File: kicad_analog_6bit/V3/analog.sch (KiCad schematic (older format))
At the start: 30 parts, among them P1 Conn_02x05_Odd_Even, P2 Conn_01x04, P3 Conn_01x06, P4 Conn_01x02, P6 Conn_01x01, P7 Conn_01x01, U1 MAX9144, U2 MAX9144, U3 DG441xY, U4 MAX5259EEE+, U5 MCP1754S-3302xCB

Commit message: Analog V3 non-inverted 14 pin
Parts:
- removed U3: DG441xY, Package_SO:SOIC-16_3.9x9.9mm_P1.27mm, symbol Analog_Switch:DG441xY
- added R10, R9: 1K, Resistor_SMD:R_0805_2012Metric_Pad1.15x1.40mm_HandSolder, symbol Device:R_Small
- added U3: 4066, Package_SO:SOIC-14_3.9x8.7mm_P1.27mm, symbol 4xxx:4066
- R1: value 150R -> 75R
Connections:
- wire segments 167 -> 166
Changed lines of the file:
@@
 Wire Wire Line
 	6450 4150 7000 4150
-Text Label 2400 6500 0    50   ~ 0
+Text Label 1400 6500 2    50   ~ 0
 GND
 Text Label 2400 5300 2    50   ~ 0
@@
 Wire Wire Line
 	6400 7550 6450 7550
-Text Label 1050 2350 2    50   ~ 0
+$Comp
+L 4xxx:4066 U3
+U 5 1 5E118FBF
+P 9050 5900
+F 0 "U3" H 9280 5946 50  0000 L CNN
+F 1 "4066" H 9280 5855 50  0000 L CNN
+F 2 "Package_SO:SOIC-14_3.9x8.7mm_P1.27mm" H 9050 5900 50  0001 C CNN
+F 3 "http://www.ti.com/lit/ds/symlink/cd4066b.pdf" H 9050 5900 50  0001 C CNN
+	5    9050 5900
+	1    0    0    -1
+$EndComp
+Text Label 9050 5400 2    50   ~ 0
 VCC
-Text Label 1050 3350 2    50   ~ 0
-GND
+Text Label 9050 6400 2    50   ~ 0
+GND
+$Comp
+L 4xxx:4066 U3
+U 1 1 5E1234E2
+P 2400 3550
+F 0 "U3" V 2354 3422 50  0000 R CNN
+F 1 "4066" V 2445 3422 50  0000 R CNN
+F 2 "Package_SO:SOIC-14_3.9x8.7mm_P1.27mm" H 2400 3550 50  0001 C CNN
+F 3 "http://www.ti.com/lit/ds/symlink/cd4066b.pdf" H 2400 3550 50  0001 C CNN
+	1    2400 3550
+	0    -1   1    0
+$EndComp
+$Comp
+L 4xxx:4066 U3
+U 2 1 5E127744
+P 4600 3550
+F 0 "U3" V 4554 3422 50  0000 R CNN
+F 1 "4066" V 4645 3422 50  0000 R CNN
+F 2 "Package_SO:SOIC-14_3.9x8.7mm_P1.27mm" H 4600 3550 50  0001 C CNN
+F 3 "http://www.ti.com/lit/ds/symlink/cd4066b.pdf" H 4600 3550 50  0001 C CNN
+	2    4600 3550
+	0    1    1    0
+$EndComp
+$Comp
+L 4xxx:4066 U3
+U 3 1 5E129BF6
+P 3150 3550
+F 0 "U3" V 3104 3422 50  0000 R CNN
+F 1 "4066" V 3195 3422 50  0000 R CNN
+F 2 "Package_SO:SOIC-14_3.9x8.7mm_P1.27mm" H 3150 3550 50  0001 C CNN
+F 3 "http://www.ti.com/lit/ds/symlink/cd4066b.pdf" H 3150 3550 50  0001 C CNN
+	3    3150 3550
+	0    1    1    0
+$EndComp
 Wire Wire Line
 	2400 3850 2400 5050
@@
 	3150 4200 3450 4200
 Wire Wire Line
+	3900 4200 3900 3850
+Wire Wire Line
+	3900 4200 4200 4200
+Wire Wire Line
 	4600 4200 4600 3850
+Connection ~ 3900 4200
 Text Label 2950 4200 2    50   ~ 0
 GND
@@
 P 2400 3000
 F 0 "R1" H 2150 3050 50  0000 L CNN
-F 1 "150R" H 2100 2950 50  0000 L CNN
+F 1 "75R" H 2100 2950 50  0000 L CNN
 F 2 "Resistor_SMD:R_0805_2012Metric_Pad1.15x1.40mm_HandSolder" H 2400 3000 50  0001 C CNN
 F 3 "~" H 2400 3000 50  0001 C CNN
@@
 Connection ~ 3450 4200
 Wire Wire Line
+	3450 4200 3900 4200
+Wire Wire Line
 	4200 4100 4200 4200
 Connection ~ 4200 4200
@@
 Wire Wire Line
 	4200 3900 4200 3800
+Connection ~ 3450 3550
+Wire Wire Line
+	3450 3550 3450 3800
 Wire Wire Line
 	4050 3800 4200 3800
+Connection ~ 4200 3800
+Wire Wire Line
+	4200 3800 4200 3550
 Wire Wire Line
 	3150 3250 3150 2450
 Connection ~ 3150 2450
 Wire Wire Line
+	3900 3250 3900 2100
+Wire Wire Line
 	4600 3250 4600 1750
 Connection ~ 4600 1750
 Wire Wire Line
+	3450 3100 3450 3550
+Wire Wire Line
 	3450 3100 4900 3100
 Wire Wire Line
@@
 Wire Wire Line
 	800  5200 800  3550
+Wire Wire Line
+	800  3550 2100 3550
 Wire Wire Line
 	1100 4450 1100 4650
@@
 Text Label 2900 6100 0    50   ~ 0
 SPARE
-Text Label 2400 3200 0    50   ~ 0
+Text Label 2400 3250 0    50   ~ 0
 SW_CLAMP
 Text Label 1950 4850 0    50   ~ 0
@@
 	1    0    0    -1
 $EndComp
+$Comp
+L 4xxx:4066 U3
+U 4 1 5E12E54E
+P 3900 3550
+F 0 "U3" V 3854 3422 50  0000 R CNN
+F 1 "4066" V 3945 3422 50  0000 R CNN
+F 2 "Package_SO:SOIC-14_3.9x8.7mm_P1.27mm" H 3900 3550 50  0001 C CNN
+F 3 "http://www.ti.com/lit/ds/symlink/cd4066b.pdf" H 3900 3550 50  0001 C CNN
+	4    3900 3550
+	0    1    1    0
+$EndComp
 Wire Wire Line
 	950  6000 1500 6000
@@
 Wire Wire Line
 	1500 6000 1900 6000
-Wire Wire Line
-	3450 3100 3450 3550
-Wire Wire Line
-	3450 4200 3900 4200
-Wire Wire Line
-	3900 4200 3900 3850
-Connection ~ 3900 4200
-Wire Wire Line
-	3900 4200 4200 4200
-Wire Wire Line
-	4800 3550 4900 3550
-Wire Wire Line
-	4200 3800 4200 3550
-Wire Wire Line
-	4200 3550 4100 3550
-Connection ~ 4200 3800
-Wire Wire Line
-	3350 3550 3450 3550
-Connection ~ 3450 3550
-Wire Wire Line
-	3450 3550 3450 3800
-Wire Wire Line
-	3900 2100 3900 3250
-Wire Wire Line
-	800  3550 2200 3550
-Wire Wire Line
-	1400 2350 1300 2350
-Connection ~ 1300 2350
-Wire Wire Line
-	1300 2350 1050 2350
-Wire Wire Line
-	1400 3350 1300 3350
-Connection ~ 1300 3350
-Wire Wire Line
-	1300 3350 1050 3350
-$Comp
-L Analog_Switch:DG441xY U3
-U 5 1 5E5EA56F
-P 1300 2850
-F 0 "U3" H 1580 2896 50  0000 L CNN
-F 1 "DG441xY" H 1580 2805 50  0000 L CNN
-F 2 "Package_SO:SOIC-16_3.9x9.9mm_P1.27mm" H 1300 2750 50  0001 C CNN
-F 3 "https://datasheets.maximintegrated.com/en/ds/DG441-DG442.pdf" H 1300 2850 50  0001 C CNN
-	5    1300 2850
-	1    0    0    -1
-$EndComp
-$Comp
-L Analog_Switch:DG441xY U3
-U 4 1 5E5EE151
-P 3900 3550
-F 0 "U3" V 3946 3680 50  0000 L CNN
-F 1 "DG441xY" V 3855 3680 50  0000 L CNN
-F 2 "Package_SO:SOIC-16_3.9x9.9mm_P1.27mm" H 3900 3450 50  0001 C CNN
-F 3 "https://datasheets.maximintegrated.com/en/ds/DG441-DG442.pdf" H 3900 3550 50  0001 C CNN
-	4    3900 3550
-	0    -1   -1   0
-$EndComp
-$Comp
-L Analog_Switch:DG441xY U3
-U 1 1 5E5EFEBA
-P 2400 3550
-F 0 "U3" V 2500 3250 50  0000 L CNN
-F 1 "DG441xY" V 2650 3050 50  0000 L CNN
-F 2 "Package_SO:SOIC-16_3.9x9.9mm_P1.27mm" H 2400 3450 50  0001 C CNN
-F 3 "https://datasheets.maximintegrated.com/en/ds/DG441-DG442.pdf" H 2400 3550 50  0001 C CNN
-	1    2400 3550
-	0    1    1    0
-$EndComp
-$Comp
-L Analog_Switch:DG441xY U3
-U 2 1 5E5F16C1
-P 4600 3550
-F 0 "U3" V 4646 3680 50  0000 L CNN
-F 1 "DG441xY" V 4555 3680 50  0000 L CNN
-F 2 "Package_SO:SOIC-16_3.9x9.9mm_P1.27mm" H 4600 3450 50  0001 C CNN
-F 3 "https://datasheets.maximintegrated.com/en/ds/DG441-DG442.pdf" H 4600 3550 50  0001 C CNN
-	2    4600 3550
-	0    -1   -1   0
-$EndComp
-$Comp
-L Analog_Switch:DG441xY U3
-U 3 1 5E5F2F3B
-P 3150 3550
-F 0 "U3" V 3196 3680 50  0000 L CNN
-F 1 "DG441xY" V 3105 3680 50  0000 L CNN
-F 2 "Package_SO:SOIC-16_3.9x9.9mm_P1.27mm" H 3150 3450 50  0001 C CNN
-F 3 "https://datasheets.maximintegrated.com/en/ds/DG441-DG442.pdf" H 3150 3550 50  0001 C CNN
-	3    3150 3550
-	0    -1   -1   0
-$EndComp
-Wire Wire Line
-	1400 2350 1400 2450
+$Comp
+L Device:R_Small R9
+U 1 1 5E6BC038
+P 1500 6300
+F 0 "R9" H 1350 6350 50  0000 L CNN
+F 1 "1K" H 1350 6250 50  0000 L CNN
+F 2 "Resistor_SMD:R_0805_2012Metric_Pad1.15x1.40mm_HandSolder" H 1500 6300 50  0001 C CNN
+F 3 "~" H 1500 6300 50  0001 C CNN
+	1    1500 6300
+	1    0    0    -1
+$EndComp
+$Comp
+L Device:R_Small R10
+U 1 1 5E6BCBE0
+P 1650 6300
+F 0 "R10" H 1709 6346 50  0000 L CNN
+F 1 "1K" H 1709 6255 50  0000 L CNN
+F 2 "Resistor_SMD:R_0805_2012Metric_Pad1.15x1.40mm_HandSolder" H 1650 6300 50  0001 C CNN
+F 3 "~" H 1650 6300 50  0001 C CNN
+	1    1650 6300
+	1    0    0    -1
+$EndComp
+Wire Wire Line
+	1500 6000 1500 6200
+Wire Wire Line
+	1650 5900 1650 6200
+Wire Wire Line
+	2400 6500 1650 6500
+Wire Wire Line
+	1500 6500 1500 6400
+Wire Wire Line
+	1650 6400 1650 6500
+Connection ~ 1650 6500
+Wire Wire Line
+	1650 6500 1500 6500
+Wire Wire Line
+	1500 6500 1400 6500
+Connection ~ 1500 6500
 $EndSCHEMATC

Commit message: V3 PCB layout with MAX4610
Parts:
- added J1: Spare DAC, TestPoint:TestPoint_Pad_D1.0mm, symbol Connector_Generic:Conn_01x01
- U1, U2: value MAX9144 -> MAX9108; symbol Comparator:MAX9144 -> analog-rescue:MAX9108-Comparator
- U3: value 4066 -> MAX4610; symbol 4xxx:4066 -> analog-rescue:MAX4610-4xxx
- renumbered C8 to C4, C9 to C5, C5 to C7, C7 to C8, C4 to C9, CL1 to Cx1, R3 to R1, R9 to R3, R10 to R4, R8 to R5, R7 to R6, R4 to R7, R5 to R8, R6 to R9, R1 to Rx1
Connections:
- wire segments 166 -> 171

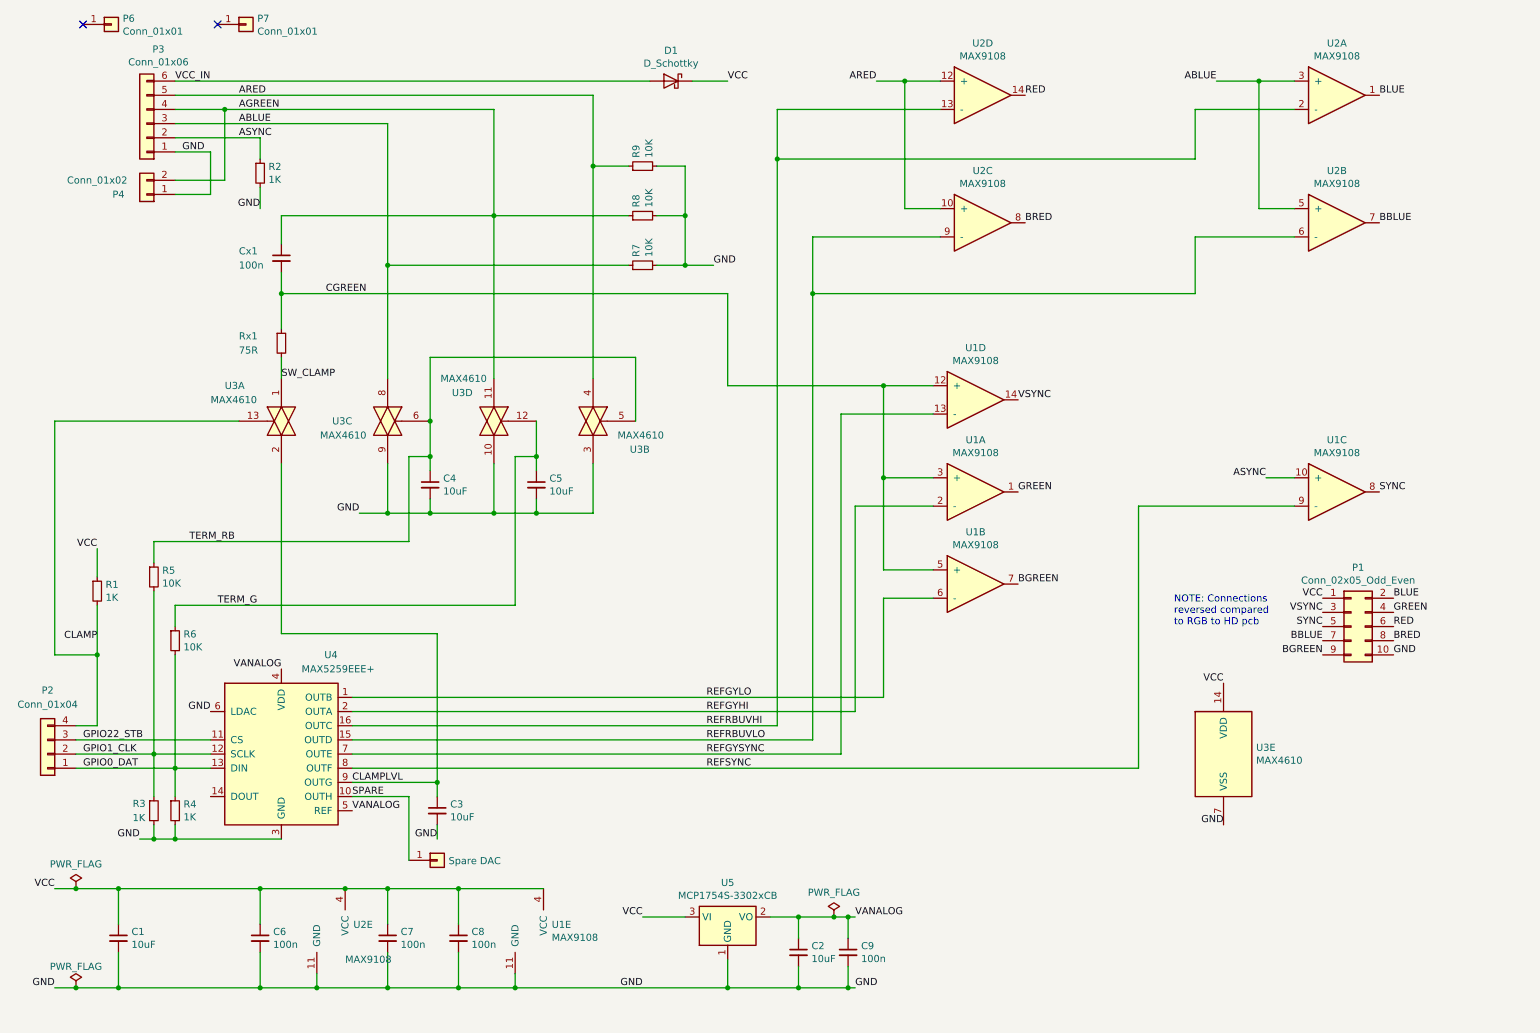
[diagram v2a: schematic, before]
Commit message: Update pcb with AC/DC switch
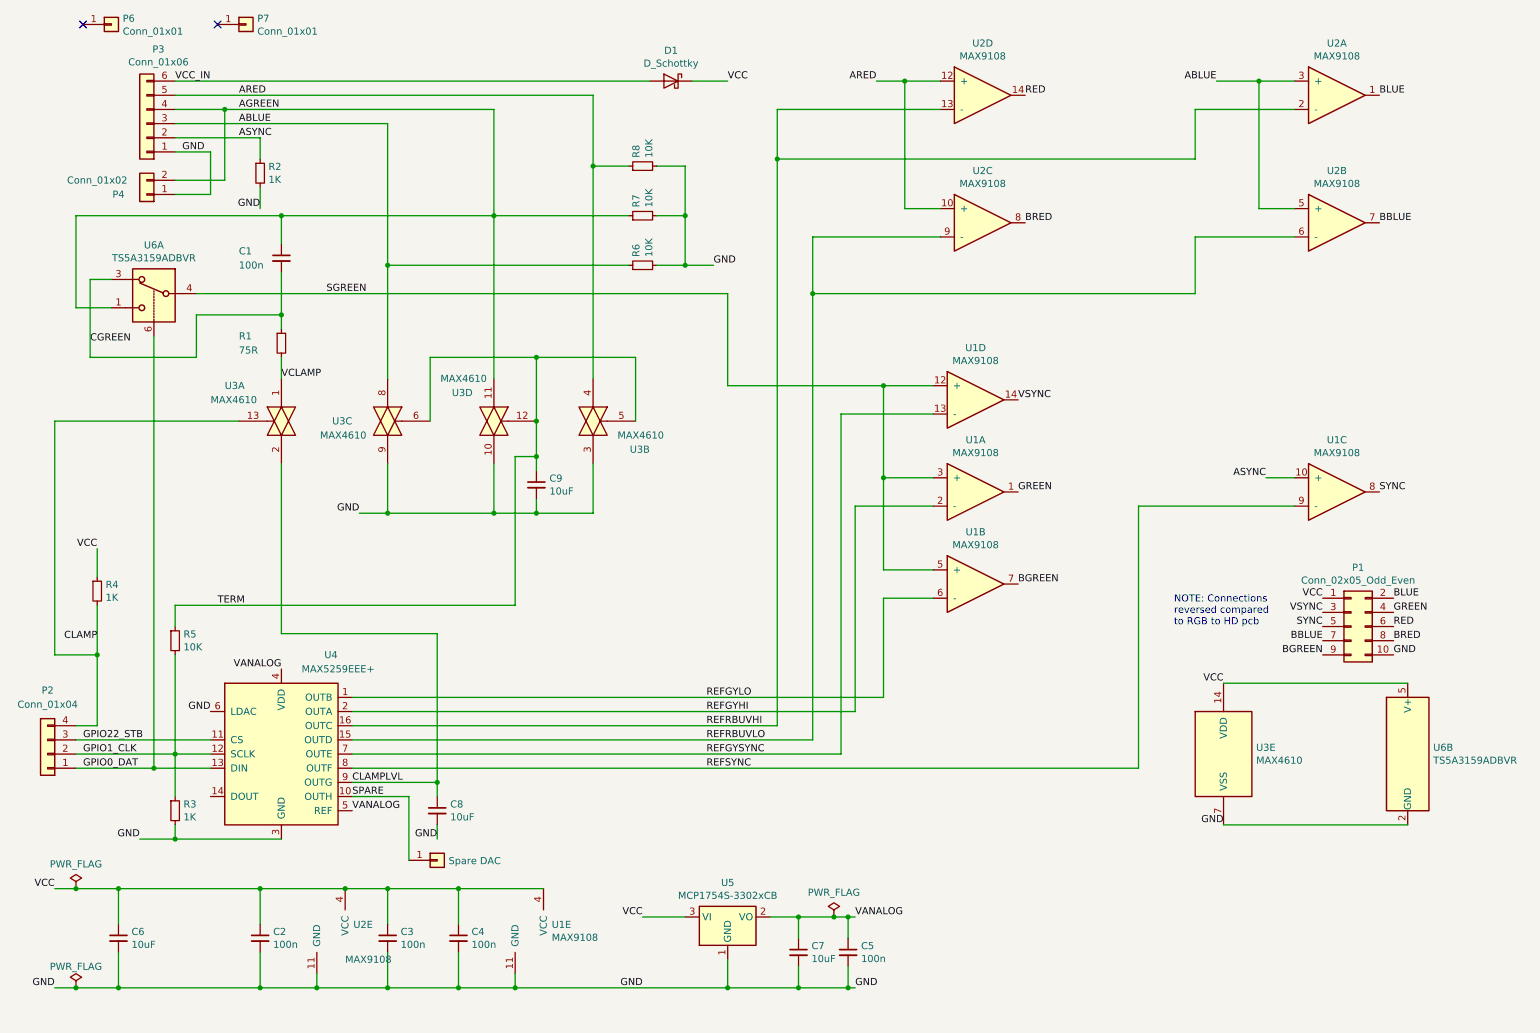
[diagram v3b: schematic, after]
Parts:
- removed C4: 10uF, Capacitor_SMD:C_0805_2012Metric_Pad1.15x1.40mm_HandSolder, symbol Device:C_Small
- removed R3: 1K, Resistor_SMD:R_0805_2012Metric_Pad1.15x1.40mm_HandSolder, symbol Device:R_Small
- removed R5: 10K, Resistor_SMD:R_0805_2012Metric_Pad1.15x1.40mm_HandSolder, symbol Device:R_Small
- added U6: TS5A3159ADBVR, Package_TO_SOT_SMD:SOT-23-6_Handsoldering, symbol Analog_Switch:TS5A3159ADBVR
- renumbered Cx1 to C1, C6 to C2, C7 to C3, C8 to C4, C9 to C5, C1 to C6, C2 to C7, C3 to C8, C5 to C9, Rx1 to R1, R4 to R3, R1 to R4, R6 to R5, R7 to R6, R8 to R7, R9 to R8
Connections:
- net TERM_RB is gone; now on net TERM: U3.5, U3.6
- net AGREEN: now also U6.1
- net CGREEN: now also U6.3; no longer U1.12 (+), U1.3 (+), U1.5 (+)
- net GND: now also U6.2 (GND)
- net GPIO0_DAT: now also U6.6; no longer R3.1, R5.2
- net GPIO1_CLK: now also R3.1, R5.2
- net VCC: now also U6.5 (V+)
- net SW_CLAMP renamed VCLAMP
- net TERM_G renamed TERM
- new net SGREEN: U1.12 (+), U1.3 (+), U1.5 (+), U6.4

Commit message: V3 pcb plus some older alternatives
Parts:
- removed J1: Spare DAC, TestPoint:TestPoint_Pad_D1.0mm, symbol Connector_Generic:Conn_01x01
- removed P1: Conn_02x05_Odd_Even, Connector_PinSocket_2.54mm:PinSocket_2x05_P2.54mm_Horizontal, symbol Connector_Generic:Conn_02x05_Odd_Even
- removed P4: Conn_01x02, Connector_PinHeader_2.54mm:PinHeader_1x02_P2.54mm_Vertical, symbol Connector_Generic:Conn_01x02
- added JP1, JP2: SolderJumper_3_Bridged12, Jumper:SolderJumper-3_P1.3mm_Bridged12_RoundedPad1.0x1.5mm, symbol Jumper:SolderJumper_3_Bridged12
- added P1: Conn_02x06_Odd_Even, Connector_PinSocket_2.54mm:PinSocket_2x06_P2.54mm_Horizontal, symbol Connector_Generic:Conn_02x06_Odd_Even
- added R10, R11, R9: 68R, Resistor_SMD:R_0805_2012Metric_Pad1.15x1.40mm_HandSolder, symbol Device:R_Small
- added U7: MAX9108-Comparator, Package_SO:SOIC-14_3.9x8.7mm_P1.27mm, symbol analog-rescue:MAX9108-Comparator
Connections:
- net ABLUE: now also R9.1, U7.10 (+), U7.12 (+); no longer U3.8
- net AGREEN: now also U6.3, R10.1; no longer U3.11, U6.1
- net ARED: now also R11.1, U7.3 (+), U7.5 (+); no longer U3.4
- net BBLUE: now also P1.7 (Pin_7)
- net BGREEN: now also P1.9 (Pin_9)
- net BLUE: now also P1.2 (Pin_2)
- net BRED: now also P1.8 (Pin_8)
- net CGREEN: now also U6.1; no longer U6.3
- net CLAMPLVL: now also U7.6 (-), U7.9 (-)
- net GND: now also P1.10 (Pin_10), U7.11 (GND)
- net GREEN: now also P1.4 (Pin_4)
- net RED: now also P1.6 (Pin_6)
- net SPARE: now also U7.13 (-), U7.2 (-)
- net SYNC: now also P1.5 (Pin_5)
- net VCC: now also P1.1 (Pin_1), U7.4 (VCC)
- net VSYNC: now also P1.3 (Pin_3)
- new net: R11.2, U3.4
- new net: R9.2, U3.8
- new net: R10.2, U3.11
- new net: JP1.1 (A), U7.14
- new net: JP1.3 (B), U7.1
- new net: JP2.1 (A), U7.7
- new net: JP2.3 (B), U7.8
- new net UV1: JP1.2 (C), P1.11 (Pin_11)
- new net UV2: JP2.2 (C), P1.12 (Pin_12)
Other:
- moved on the sheet: C8, U1C, U2B, U2C

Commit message: Updated analog board
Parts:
- R10, R11, R9: value 68R -> 75R
- R6, R7, R8: value 10K -> 47K
- U3: value MAX4610 -> TS12A44514DR; symbol analog-rescue:MAX4610-4xxx -> analog-rescue:TS12A44514DR-4xxx
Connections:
- net UV1: now also JP2.2 (C), P1.12 (Pin_12); no longer JP1.2 (C), P1.11 (Pin_11)
- net UV2: now also JP1.2 (C), P1.11 (Pin_11); no longer JP2.2 (C), P1.12 (Pin_12)
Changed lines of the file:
@@
 	6400 7550 6450 7550
 $Comp
-L analog-rescue:MAX4610-4xxx U3
+L analog-rescue:TS12A44514DR-4xxx U3
 U 5 1 5E118FBF
 P 9050 5900
 F 0 "U3" H 9280 5946 50  0000 L CNN
-F 1 "MAX4610" H 9280 5855 50  0000 L CNN
+F 1 "TS12A44514DR" H 9280 5855 50  0000 L CNN
 F 2 "Package_SO:SOIC-14_3.9x8.7mm_P1.27mm" H 9050 5900 50  0001 C CNN
-F 3 "http://www.ti.com/lit/ds/symlink/cdMAX4610b.pdf" H 9050 5900 50  0001 C CNN
+F 3 "http://www.ti.com/lit/ds/symlink/cdTS12A44514DRb.pdf" H 9050 5900 50  0001 C CNN
 	5    9050 5900
 	1    0    0    -1
@@
 GND
 $Comp
-L analog-rescue:MAX4610-4xxx U3
+L analog-rescue:TS12A44514DR-4xxx U3
 U 1 1 5E1234E2
 P 2400 3550
 F 0 "U3" V 2150 3950 50  0000 R CNN
-F 1 "MAX4610" V 2250 4050 50  0000 R CNN
+F 1 "TS12A44514DR" V 2250 4250 50  0000 R CNN
 F 2 "Package_SO:SOIC-14_3.9x8.7mm_P1.27mm" H 2400 3550 50  0001 C CNN
-F 3 "http://www.ti.com/lit/ds/symlink/cdMAX4610b.pdf" H 2400 3550 50  0001 C CNN
+F 3 "http://www.ti.com/lit/ds/symlink/cdTS12A44514DRb.pdf" H 2400 3550 50  0001 C CNN
 	1    2400 3550
 	0    -1   1    0
 $EndComp
 $Comp
-L analog-rescue:MAX4610-4xxx U3
+L analog-rescue:TS12A44514DR-4xxx U3
 U 2 1 5E127744
 P 4600 3550
 F 0 "U3" V 4800 3950 50  0000 R CNN
-F 1 "MAX4610" V 4700 4050 50  0000 R CNN
+F 1 "TS12A44514DR" V 4900 4150 50  0000 R CNN
 F 2 "Package_SO:SOIC-14_3.9x8.7mm_P1.27mm" H 4600 3550 50  0001 C CNN
-F 3 "http://www.ti.com/lit/ds/symlink/cdMAX4610b.pdf" H 4600 3550 50  0001 C CNN
+F 3 "http://www.ti.com/lit/ds/symlink/cdTS12A44514DRb.pdf" H 4600 3550 50  0001 C CNN
 	2    4600 3550
 	0    1    1    0
 $EndComp
 $Comp
-L analog-rescue:MAX4610-4xxx U3
+L analog-rescue:TS12A44514DR-4xxx U3
 U 3 1 5E129BF6
 P 3150 3550
-F 0 "U3" V 3150 3300 50  0000 R CNN
-F 1 "MAX4610" V 3250 3400 50  0000 R CNN
+F 0 "U3" V 3350 3300 50  0000 R CNN
+F 1 "TS12A44514DR" V 3450 3500 50  0000 R CNN
 F 2 "Package_SO:SOIC-14_3.9x8.7mm_P1.27mm" H 3150 3550 50  0001 C CNN
-F 3 "http://www.ti.com/lit/ds/symlink/cdMAX4610b.pdf" H 3150 3550 50  0001 C CNN
+F 3 "http://www.ti.com/lit/ds/symlink/cdTS12A44514DRb.pdf" H 3150 3550 50  0001 C CNN
 	3    3150 3550
 	0    1    1    0
@@
 P 4950 2450
 F 0 "R6" H 5009 2496 50  0000 L CNN
-F 1 "10K" H 5009 2405 50  0000 L CNN
+F 1 "47K" H 5009 2405 50  0000 L CNN
 F 2 "Resistor_SMD:R_0805_2012Metric_Pad1.15x1.40mm_HandSolder" H 4950 2450 50  0001 C CNN
 F 3 "~" H 4950 2450 50  0001 C CNN
@@
 P 4950 2100
 F 0 "R7" H 5009 2146 50  0000 L CNN
-F 1 "10K" H 5009 2055 50  0000 L CNN
+F 1 "47K" H 5009 2055 50  0000 L CNN
 F 2 "Resistor_SMD:R_0805_2012Metric_Pad1.15x1.40mm_HandSolder" H 4950 2100 50  0001 C CNN
 F 3 "~" H 4950 2100 50  0001 C CNN
@@
 P 4950 1750
 F 0 "R8" H 5009 1796 50  0000 L CNN
-F 1 "10K" H 5009 1705 50  0000 L CNN
+F 1 "47K" H 5009 1705 50  0000 L CNN
 F 2 "Resistor_SMD:R_0805_2012Metric_Pad1.15x1.40mm_HandSolder" H 4950 1750 50  0001 C CNN
 F 3 "~" H 4950 1750 50  0001 C CNN
@@
 	1650 4850 1650 5000
 $Comp
-L analog-rescue:MAX4610-4xxx U3
+L analog-rescue:TS12A44514DR-4xxx U3
 U 4 1 5E12E54E
 P 3900 3550
-F 0 "U3" V 3700 3400 50  0000 R CNN
-F 1 "MAX4610" V 3600 3500 50  0000 R CNN
+F 0 "U3" V 4100 3250 50  0000 R CNN
+F 1 "TS12A44514DR" V 4200 3450 50  0000 R CNN
 F 2 "Package_SO:SOIC-14_3.9x8.7mm_P1.27mm" H 3900 3550 50  0001 C CNN
-F 3 "http://www.ti.com/lit/ds/symlink/cdMAX4610b.pdf" H 3900 3550 50  0001 C CNN
+F 3 "http://www.ti.com/lit/ds/symlink/cdTS12A44514DRb.pdf" H 3900 3550 50  0001 C CNN
 	4    3900 3550
 	0    1    1    0
@@
 P 3900 2850
 F 0 "R10" H 3959 2896 50  0000 L CNN
-F 1 "68R" H 3959 2805 50  0000 L CNN
+F 1 "75R" H 3959 2805 50  0000 L CNN
 F 2 "Resistor_SMD:R_0805_2012Metric_Pad1.15x1.40mm_HandSolder" H 3900 2850 50  0001 C CNN
 F 3 "~" H 3900 2850 50  0001 C CNN
@@
 P 4600 2850
 F 0 "R11" H 4659 2896 50  0000 L CNN
-F 1 "68R" H 4659 2805 50  0000 L CNN
+F 1 "75R" H 4659 2805 50  0000 L CNN
 F 2 "Resistor_SMD:R_0805_2012Metric_Pad1.15x1.40mm_HandSolder" H 4600 2850 50  0001 C CNN
 F 3 "~" H 4600 2850 50  0001 C CNN
@@
 P 3150 2850
 F 0 "R9" H 3209 2896 50  0000 L CNN
-F 1 "68R" H 3209 2805 50  0000 L CNN
+F 1 "75R" H 3209 2805 50  0000 L CNN
 F 2 "Resistor_SMD:R_0805_2012Metric_Pad1.15x1.40mm_HandSolder" H 3150 2850 50  0001 C CNN
 F 3 "~" H 3150 2850 50  0001 C CNN
@@
 	10700 2900 10750 2900
 Text Label 10900 4200 0    50   ~ 0
+UV1
+Text Label 10900 3100 0    50   ~ 0
 UV2
-Text Label 10900 3100 0    50   ~ 0
+Text Label 10150 5200 0    50   ~ 0
 UV1
-Text Label 10150 5200 0    50   ~ 0
+Text Label 9650 5200 2    50   ~ 0
 UV2
-Text Label 9650 5200 2    50   ~ 0
-UV1
 Wire Wire Line
 	9100 3950 9350 3950
